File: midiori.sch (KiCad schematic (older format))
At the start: 17 parts, among them U1 74LS245, U14 7407, U15 74LS157, U2 74LS133, U3 74LS133, U4 74LS08, U6 ym3802-x, U7 74LS32, U8 74LS04, U9 74LS10, X1 CXO_DIP8, X2 CXO_DIP8

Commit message: finish
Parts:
- added C? (x16): u1, symbol Device:C
- added J? (x3): DIN-5_180degree, symbol Connector:DIN-5_180degree
- added JP1: Jumper_3_Bridged12, symbol Jumper:Jumper_3_Bridged12
- added JP?: Jumper_NO_Small, symbol Device:Jumper_NO_Small
- added R1, R3, R5: 10K, symbol Device:R
- added R28: 270, symbol Device:R
- added R29: 220i, symbol Device:R
- added R6, R7, R8, R9: 220, symbol Device:R
- added U10: 74LS393, symbol 74xx:74LS393
- added U11: 74LS74, symbol 74xx:74LS74
- added unit 6 of U14
- added unit 1 of U14
- added unit 5 of U4
- added U5: 74LS38, symbol 74xx:74LS38
- added unit 1 of U7
- added unit 5 of U7
- added unit 3 of U8
- added unit 2 of U8
- added unit 6 of U8
- added unit 7 of U8
- added U?: H11L1, symbol Isolator:H11L1
- added U?: 74LS04, symbol 74xx:74LS04
- J?: symbol x68k:x68000_expansion -> midiori-rescue:x68000_expansion-x68k
- U6: symbol x68k:ym3802-x -> midiori-rescue:ym3802-x-x68k
- gave numbers to parts that had none: 3
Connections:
- net labels added: 4MHz
- wire segments 93 -> 251
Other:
- moved on the sheet: U2B, U3B, U9D, X1, X2

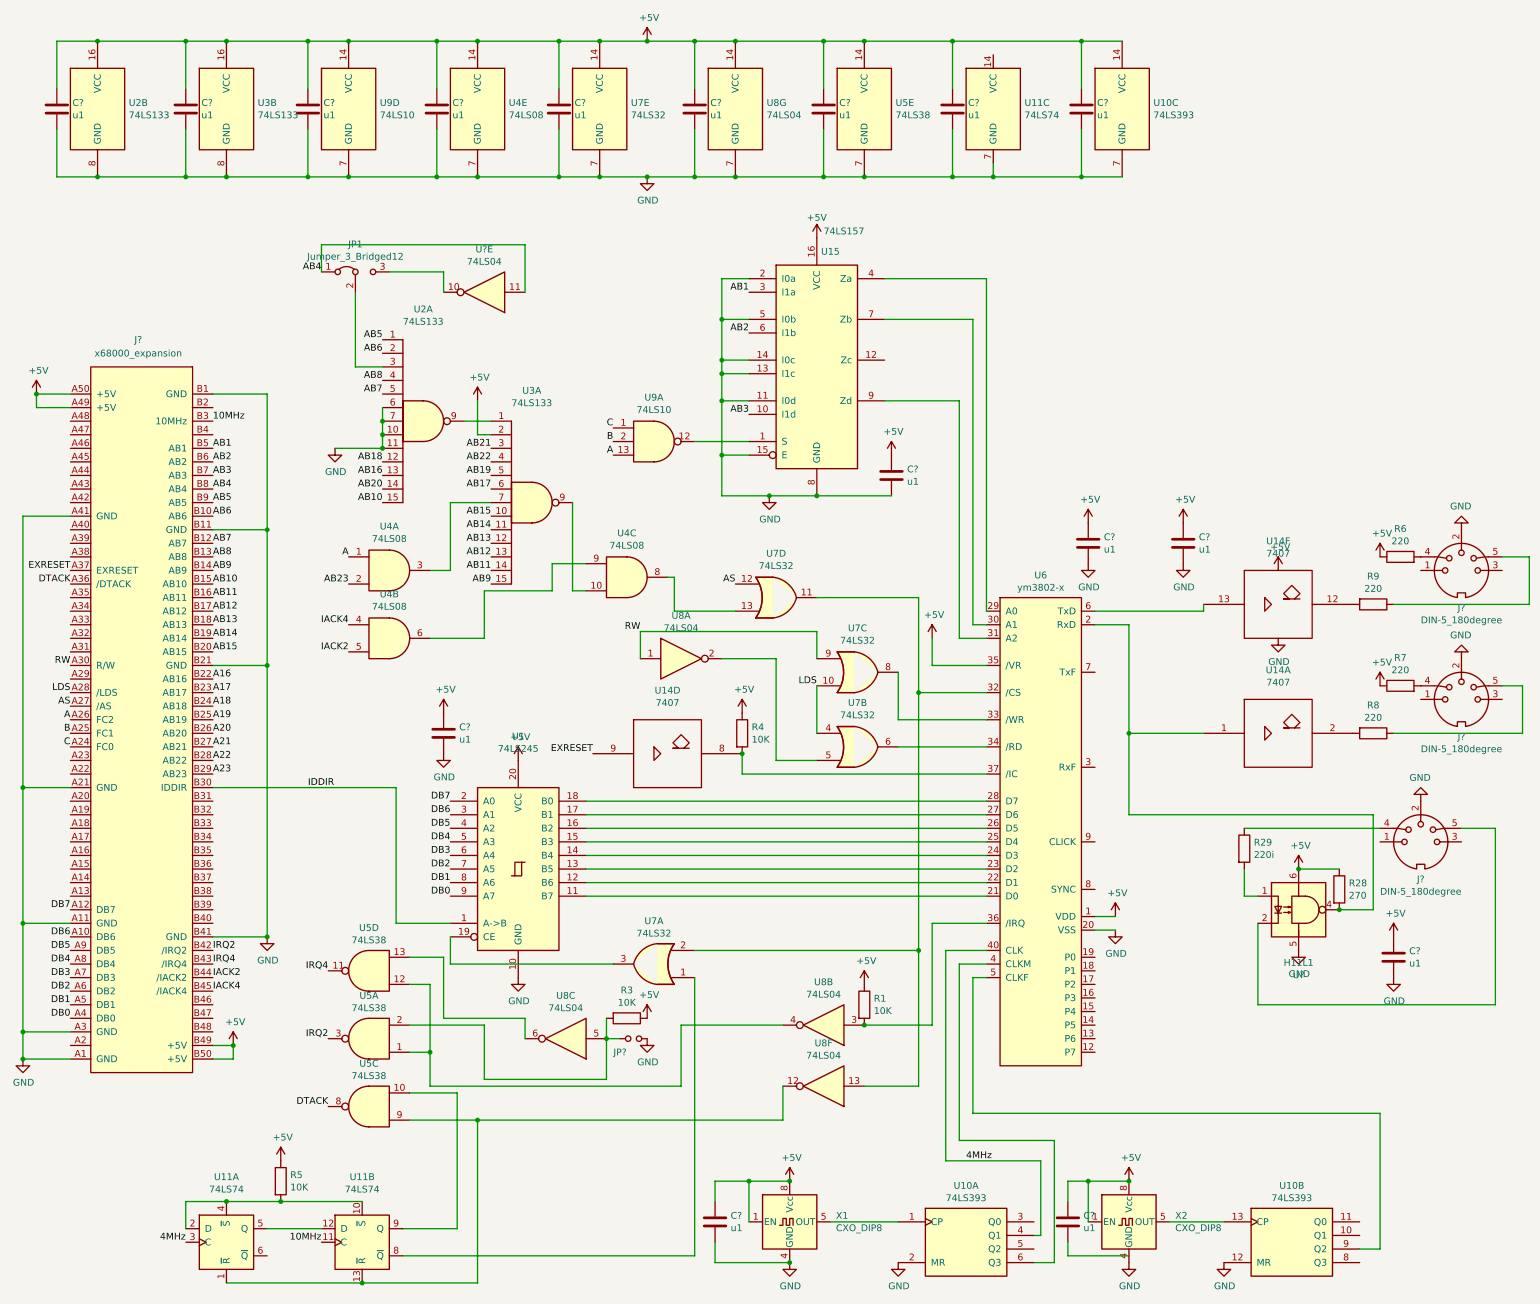
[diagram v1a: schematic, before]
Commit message: Add footprints
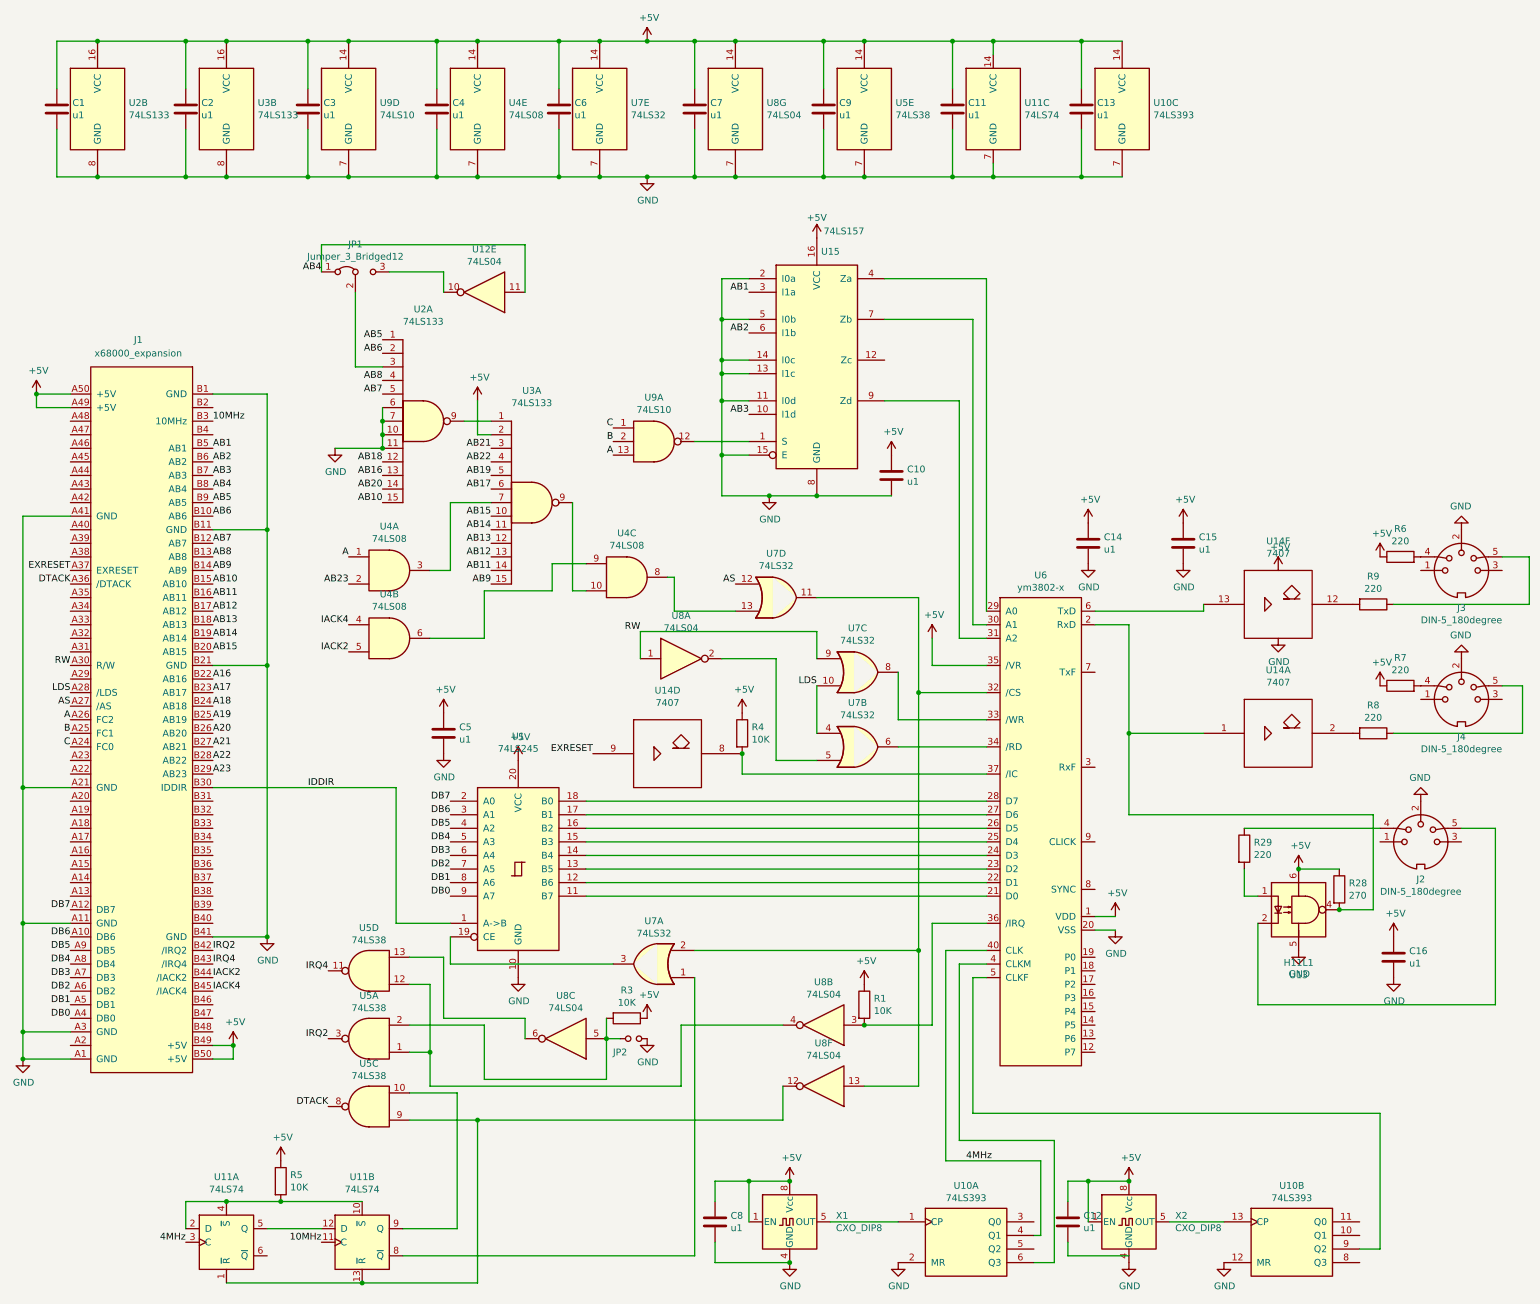
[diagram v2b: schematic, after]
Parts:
- C1, C10, C11, C12, C13, C14, C15, C16, C2, C3, C4, C5, C6, C7, C8, C9: renamed from C?; footprint (none) -> Capacitor_SMD:C_0805_2012Metric_Pad1.15x1.40mm_HandSolder
- JP1: footprint (none) -> Connector_PinHeader_2.54mm:PinHeader_1x03_P2.54mm_Vertical
- JP2: renamed from JP?; footprint (none) -> Connector_PinHeader_2.54mm:PinHeader_1x02_P2.54mm_Vertical
- R1, R28, R3, R4, R5, R6, R7, R8, R9: footprint (none) -> Resistor_SMD:R_0805_2012Metric_Pad1.15x1.40mm_HandSolder
- R29: value 220i -> 220; footprint (none) -> Resistor_SMD:R_0805_2012Metric_Pad1.15x1.40mm_HandSolder
- U1: footprint (none) -> Package_SO:SOIC-20W_7.5x12.8mm_P1.27mm
- U10, U11, U14, U3, U4, U5, U7, U8, U9: footprint (none) -> Package_SO:SOIC-14_3.9x8.7mm_P1.27mm
- U12: renamed from U?; footprint (none) -> Package_SO:SOIC-14_3.9x8.7mm_P1.27mm
- U13: renamed from U?; footprint (none) -> Package_DIP:DIP-6_W8.89mm_SMDSocket_LongPads
- U15, U2: footprint (none) -> Package_SO:SOIC-16_3.9x9.9mm_P1.27mm
- U6: footprint (none) -> Package_DIP:DIP-40_W15.24mm_Socket
- gave numbers to parts that had none: 4
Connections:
- net +5V: now also U11.14 (VCC)

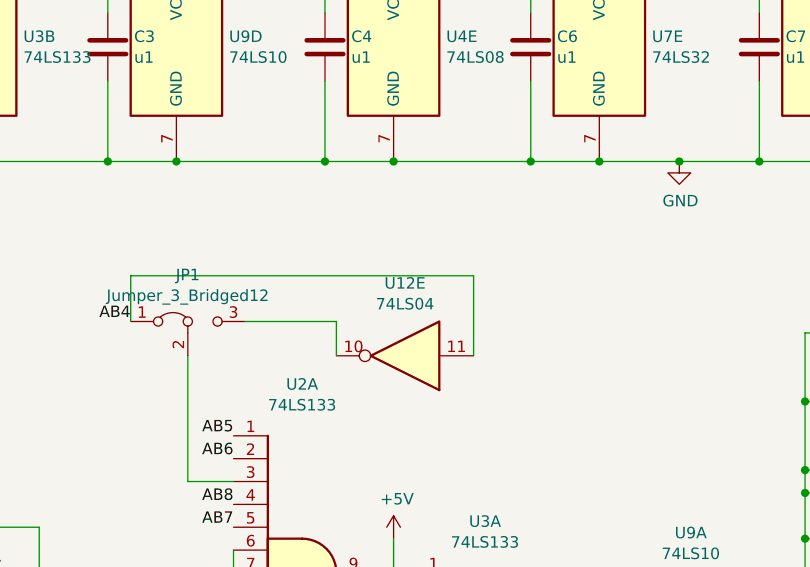
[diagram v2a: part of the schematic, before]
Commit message: Add board outline
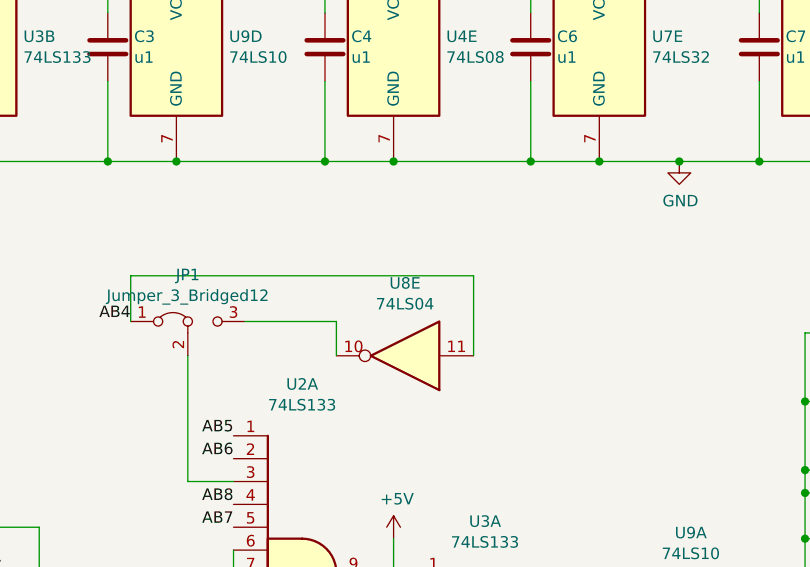
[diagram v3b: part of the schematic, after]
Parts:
- J1: footprint (none) -> x68k:x68000_expansion
- J2, J3, J4: footprint (none) -> x68k:sds-50j
- U3: footprint Package_SO:SOIC-14_3.9x8.7mm_P1.27mm -> Package_SO:SOIC-16_3.9x9.9mm_P1.27mm
- U5: footprint (none) -> Package_SO:SOIC-14_3.9x8.7mm_P1.27mm
- renumbered U12 to U8
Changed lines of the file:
@@
 F 0 "J1" H 1750 -5050 50  0000 C CNN
 F 1 "x68000_expansion" H 1750 -5150 50  0000 C CNN
-F 2 "" H 1750 -150 50  0001 C CNN
+F 2 "x68k:x68000_expansion" H 1750 -150 50  0001 C CNN
 F 3 "" H 1750 -150 50  0001 C CNN
 	1    2150 -1050
@@
 F 0 "U3" H 4650 4975 50  0000 C CNN
 F 1 "74LS133" H 4650 4884 50  0000 C CNN
-F 2 "Package_SO:SOIC-14_3.9x8.7mm_P1.27mm" H 4650 4150 50  0001 C CNN
+F 2 "Package_SO:SOIC-16_3.9x9.9mm_P1.27mm" H 4650 4150 50  0001 C CNN
 F 3 "http://www.ti.com/lit/gpn/sn74LS133" H 4650 4150 50  0001 C CNN
 	1    4650 4150
@@
 F 0 "U3" H 2630 1296 50  0000 L CNN
 F 1 "74LS133" H 2630 1205 50  0000 L CNN
-F 2 "Package_SO:SOIC-14_3.9x8.7mm_P1.27mm" H 2400 1250 50  0001 C CNN
+F 2 "Package_SO:SOIC-16_3.9x9.9mm_P1.27mm" H 2400 1250 50  0001 C CNN
 F 3 "http://www.ti.com/lit/gpn/sn74LS133" H 2400 1250 50  0001 C CNN
 	2    2400 1250
@@
 F 0 "U5" H 3450 7783 50  0000 C CNN
 F 1 "74LS38" H 3450 7874 50  0000 C CNN
-F 2 "" H 3450 8100 50  0001 C CNN
+F 2 "Package_SO:SOIC-14_3.9x8.7mm_P1.27mm" H 3450 8100 50  0001 C CNN
 F 3 "http://www.ti.com/lit/gpn/sn74LS38" H 3450 8100 50  0001 C CNN
 	1    3450 8100
@@
 F 0 "U5" H 3450 7283 50  0000 C CNN
 F 1 "74LS38" H 3450 7374 50  0000 C CNN
-F 2 "" H 3450 7600 50  0001 C CNN
+F 2 "Package_SO:SOIC-14_3.9x8.7mm_P1.27mm" H 3450 7600 50  0001 C CNN
 F 3 "http://www.ti.com/lit/gpn/sn74LS38" H 3450 7600 50  0001 C CNN
 	4    3450 7600
@@
 F 0 "U5" H 3450 8283 50  0000 C CNN
 F 1 "74LS38" H 3450 8374 50  0000 C CNN
-F 2 "" H 3450 8600 50  0001 C CNN
+F 2 "Package_SO:SOIC-14_3.9x8.7mm_P1.27mm" H 3450 8600 50  0001 C CNN
 F 3 "http://www.ti.com/lit/gpn/sn74LS38" H 3450 8600 50  0001 C CNN
 	3    3450 8600
@@
 F 0 "J3" H 11500 4375 50  0000 C CNN
 F 1 "DIN-5_180degree" H 11500 4284 50  0000 C CNN
-F 2 "" H 11500 4650 50  0001 C CNN
+F 2 "x68k:sds-50j" H 11500 4650 50  0001 C CNN
 F 3 "http://www.mouser.com/ds/2/18/40_c091_abd_e-75918.pdf" H 11500 4650 50  0001 C CNN
 	1    11500 4650
@@
 F 0 "J4" H 11500 5325 50  0000 C CNN
 F 1 "DIN-5_180degree" H 11500 5234 50  0000 C CNN
-F 2 "" H 11500 5600 50  0001 C CNN
+F 2 "x68k:sds-50j" H 11500 5600 50  0001 C CNN
 F 3 "http://www.mouser.com/ds/2/18/40_c091_abd_e-75918.pdf" H 11500 5600 50  0001 C CNN
 	1    11500 5600
@@
 F 0 "J2" H 11200 6375 50  0000 C CNN
 F 1 "DIN-5_180degree" H 11200 6284 50  0000 C CNN
-F 2 "" H 11200 6650 50  0001 C CNN
+F 2 "x68k:sds-50j" H 11200 6650 50  0001 C CNN
 F 3 "http://www.mouser.com/ds/2/18/40_c091_abd_e-75918.pdf" H 11200 6650 50  0001 C CNN
 	1    11200 6650
@@
 $EndComp
 $Comp
-L 74xx:74LS04 U12
+L 74xx:74LS04 U8
 U 5 1 5C196BCB
 P 4300 2600
-F 0 "U12" H 4300 2283 50  0000 C CNN
+F 0 "U8" H 4300 2283 50  0000 C CNN
 F 1 "74LS04" H 4300 2374 50  0000 C CNN
 F 2 "Package_SO:SOIC-14_3.9x8.7mm_P1.27mm" H 4300 2600 50  0001 C CNN
